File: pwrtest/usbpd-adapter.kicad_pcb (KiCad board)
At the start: 2 copper layers, 75.7 x 45.6 mm, 95 parts, among them J1 Conn_01x04, J2 Conn_01x04, J3 USB_C_Receptacle_USB2.0_16P, J5 Screw_Terminal_01x03, Q2 BC847, Q3 BC847, Q4 BC847, Q5 DMP3099L, Q7 BC847, Q8 BC847, U1 AP63205WU, U11 TL431, U12 TL431, U2 L7812, U4 TPS5430DDA, U5 L7905, U6 TL431DBZ, U7 TL431DBZ, U8 TL431DBZ, U9 CH224K

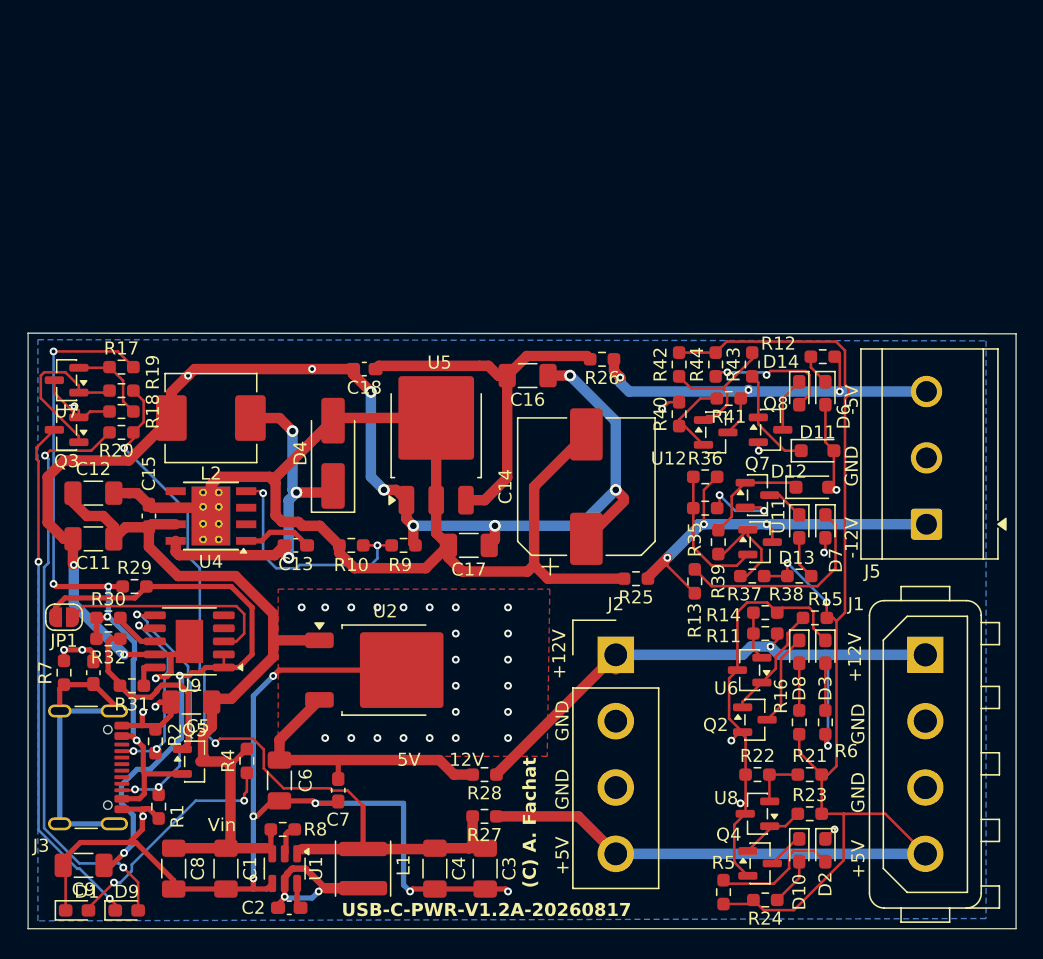
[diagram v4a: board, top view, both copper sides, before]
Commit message: updated schematics (untested)
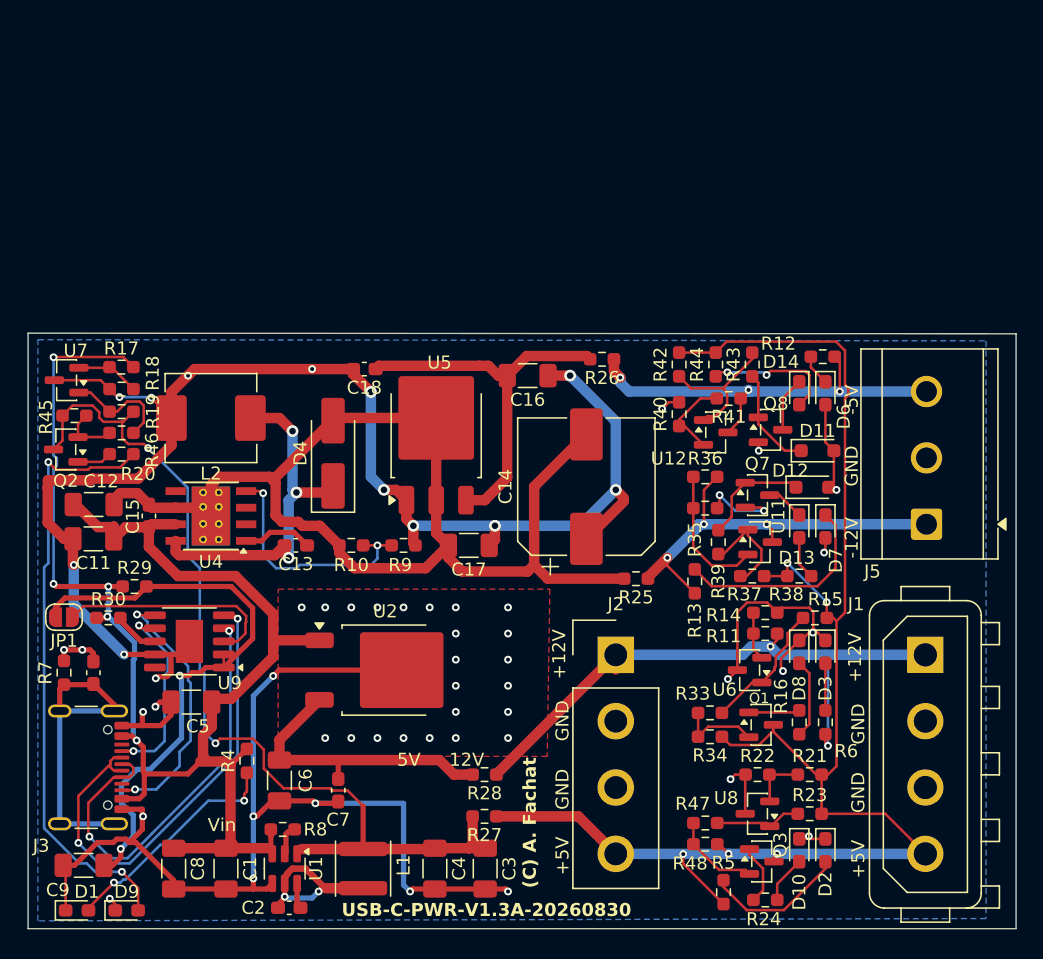
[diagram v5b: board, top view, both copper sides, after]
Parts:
- removed Q4: BC847, Package_TO_SOT_SMD:SOT-23
- removed Q5: DMP3099L, Package_TO_SOT_SMD:SOT-23
- removed R1, R2: 5.1k, Resistor_SMD:R_0603_1608Metric_Pad0.98x0.95mm_HandSolder
- removed R31, R32: 10k, Resistor_SMD:R_0603_1608Metric_Pad0.98x0.95mm_HandSolder
- added Q1: BC857, Package_TO_SOT_SMD:SOT-23, F.Cu at (141.4, 85.0)
- added R33: 10k, Resistor_SMD:R_0603_1608Metric_Pad0.98x0.95mm_HandSolder, F.Cu at (137.5, 84.1)
- added R34: 10k, Resistor_SMD:R_0603_1608Metric_Pad0.98x0.95mm_HandSolder, F.Cu at (137.5, 85.9)
- added R45: 10k, Resistor_SMD:R_0603_1608Metric_Pad0.98x0.95mm_HandSolder, F.Cu at (88.8, 61.3)
- added R46: 10k, Resistor_SMD:R_0603_1608Metric_Pad0.98x0.95mm_HandSolder, F.Cu at (92.4, 62.6)
- added R47: 10k, Resistor_SMD:R_0603_1608Metric_Pad0.98x0.95mm_HandSolder, F.Cu at (137.1, 92.5)
- added R48: 10k, Resistor_SMD:R_0603_1608Metric_Pad0.98x0.95mm_HandSolder, F.Cu at (137.1, 94.1)
- Q2, Q3: value BC847 -> BC857
- R12: value 390 -> 420
- R13: value 1.8k -> 2k2
- R15, R19, R23: value 10k -> 4k7
- R29: value 1k -> 1k, >=0.3W
- moved Q3 62.7 mm to (141.4, 95.5), turned to 0 degrees
- moved Q2 56.7 mm to (88.1, 63.9), turned to 180 degrees
- moved R18 1.72 mm to (92.4, 59.3)
- moved R20 1.66 mm to (92.4, 64.3)
- moved R19 1.61 mm to (92.4, 61.0)
- moved C12 0.87 mm to (90.3, 68.1)
- turned R24 to 0 degrees
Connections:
- C1 pad 1: VIN -> VBUS
- C11 pad 1: VIN -> VBUS
- C12 pad 1: VIN -> VBUS
- C15 pad 1: VIN -> VBUS
- C5 pad 1: VIN -> VBUS
- C8 pad 1: VIN -> VBUS
- D10 pad 1: Net-(D10-K) -> GND
- D8 pad 1: Net-(D8-K) -> GND
- D9 pad 1: Net-(D9-K) -> GND
- J3 pad A6: unconnected-(J3-D+-PadA6) -> Net-(U9-DP)
- J3 pad A7: unconnected-(J3-D--PadA7) -> Net-(U9-DM)
- J3 pad B6: unconnected-(J3-D+-PadB6) -> Net-(U9-DP)
- J3 pad B7: unconnected-(J3-D--PadB7) -> Net-(U9-DM)
- Q2 pad 1: Net-(Q2-B) -> Net-(Q2-C)
- Q2 pad 2: GND -> Net-(Q2-B)
- Q2 pad 3: Net-(D8-K) -> 5VP
- Q3 pad 1: Net-(Q3-B) -> Net-(Q3-C)
- Q3 pad 2: GND -> Net-(Q3-B)
- Q3 pad 3: Net-(D9-K) -> 5V
- R15 pad 1: Net-(Q2-B) -> Net-(U6-K)
- R16 pad 1: Net-(D8-A) -> Net-(Q1-C)
- R16 pad 2: 5V -> Net-(D8-A)
- R19 pad 1: Net-(Q3-B) -> Net-(U7-K)
- R20 pad 1: Net-(D9-A) -> Net-(Q2-C)
- R20 pad 2: 5VP -> Net-(D9-A)
- R24 pad 1: Net-(D10-A) -> Net-(Q3-C)
- R24 pad 2: 5V -> Net-(D10-A)
- R4 pad 2: VIN -> VBUS
- R8 pad 1: VIN -> VBUS
- U1 pad 3: VIN -> VBUS
- U2 pad 1: VIN -> VBUS
- U4 pad 7: VIN -> VBUS
- U6 pad 1: Net-(Q2-B) -> Net-(U6-K)
- U7 pad 1: Net-(Q3-B) -> Net-(U7-K)
- U9 pad 10: Net-(U9-PG) -> unconnected-(U9-PG-Pad10)
- U9 pad 4: unconnected-(U9-DP-Pad4) -> Net-(U9-DP)
- U9 pad 5: unconnected-(U9-DM-Pad5) -> Net-(U9-DM)
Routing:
- net VIN: track 62.9 -> 0.00 mm
- net VBUS: track 55.4 -> 117.3 mm
- net Net-(D9-K): track 40.0 -> 0.00 mm, vias 2 -> 0
- net Net-(U9-DM): track 0.00 -> 37.4 mm, vias 0 -> 2
- net Net-(U9-DP): track 0.00 -> 33.3 mm, vias 0 -> 2
- net Net-(Q5-G): track 15.6 -> 0.00 mm
- net Net-(U6-K): track 0.00 -> 10.3 mm
- net Net-(U7-K): track 0.00 -> 8.44 mm
- net 5VP: track 65.7 -> 72.9 mm
- net Net-(D8-K): track 7.10 -> 0.00 mm
- net Net-(Q1-B): track 0.00 -> 6.37 mm
- net Net-(Q3-B): track 12.7 -> 6.86 mm
- net Net-(Q3-C): track 0.00 -> 4.63 mm
- net Net-(Q2-B): track 8.77 -> 4.45 mm
- net GND: track 257.7 -> 253.5 mm, vias 55 -> 59
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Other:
- board text added: "USB-C-PWR-V1.3A-20260830"
- board text removed: "USB-C-PWR-V1.2A-20260817"

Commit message: usb pd updated
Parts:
- removed R15, R19, R23: 4k7, Resistor_SMD:R_0603_1608Metric_Pad0.98x0.95mm_HandSolder
- R16, R20, R24: value 560 -> 680
- R33, R34, R45, R46, R47, R48: value 10k -> 2k2
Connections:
- D10 pad 1: GND -> Net-(D10-K)
- D10 pad 2: Net-(D10-A) -> 5V
- D8 pad 1: GND -> Net-(D8-K)
- D8 pad 2: Net-(D8-A) -> 5V
- D9 pad 1: GND -> Net-(D9-K)
- D9 pad 2: Net-(D9-A) -> 5VP
- Q1 pad 1: Net-(Q1-C) -> Net-(D8-K)
- Q2 pad 1: Net-(Q2-C) -> Net-(D9-K)
- Q3 pad 1: Net-(Q3-C) -> Net-(D10-K)
- R16 pad 1: Net-(Q1-C) -> Net-(D8-K)
- R16 pad 2: Net-(D8-A) -> GND
- R20 pad 1: Net-(Q2-C) -> Net-(D9-K)
- R20 pad 2: Net-(D9-A) -> GND
- R24 pad 1: Net-(Q3-C) -> Net-(D10-K)
- R24 pad 2: Net-(D10-A) -> GND
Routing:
- net Net-(D9-A): track 46.2 -> 0.00 mm, vias 2 -> 0
- net Net-(D9-K): track 0.00 -> 42.0 mm, vias 0 -> 2
- net GND: track 253.5 -> 294.3 mm, vias 59 -> 65
- net 5VP: track 72.9 -> 90.0 mm, vias 2 -> 4
- net Net-(D8-K): track 0.00 -> 9.93 mm
- net Net-(D10-K): track 0.00 -> 8.77 mm
- net Net-(U6-K): track 10.3 -> 4.02 mm
- net Net-(D8-A): track 6.08 -> 0.00 mm
- net Net-(Q3-C): track 4.63 -> 0.00 mm
- net Net-(Q1-C): track 3.92 -> 0.00 mm
- net Net-(D10-A): track 3.62 -> 0.00 mm
- net Net-(U7-K): track 8.44 -> 5.58 mm
- net Net-(Q2-C): track 2.66 -> 0.00 mm
- net 5V: track 119.6 -> 122.2 mm, vias 5 -> 6
- net Net-(U8-K): track 6.66 -> 4.23 mm
